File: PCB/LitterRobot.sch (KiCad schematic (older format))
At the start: 5 parts, among them J1 DF11C-4DP-2V(57), J2 DF11C-6DP-2V(57), J3 DF11C-8DP-2V(57), J4 DF11C-6DP-2V(57)

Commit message: Cleaned up the schematics
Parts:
- F1: value Polyfuse -> 1.1A; Voltage (none) -> 24V
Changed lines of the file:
@@
 TODO_1
-$Comp
-L Device:Polyfuse F1
-U 1 1 6061774B
-P 1250 2750
-F 0 "F1" H 1338 2796 50  0000 L CNN
-F 1 "Polyfuse" H 1338 2705 50  0000 L CNN
-F 2 "LitterRobot:Bel_Fuse_0ZCG" H 1300 2550 50  0001 L CNN
-F 3 "https://www.belfuse.com/resources/datasheets/circuitprotection/ds-cp-0zcg-series.pdf" H 1250 2750 50  0001 C CNN
-F 4 "0ZCG0110BF2B" H 1250 2750 50  0001 C CNN "Part_number"
-	1    1250 2750
-	1    0    0    -1
-$EndComp
 $Comp
 L power:+15V #PWR01
@@
 F32 "Light_sensor_SCL" O L 6000 2200 50
 F33 "Light_sensor_INT" I L 6000 2300 50
+F34 "Extension1" B L 6000 3100 50
+F35 "Extension2" B L 6000 3200 50
+F36 "Extension3" B L 6000 3300 50
+F37 "Extension4" B L 6000 3400 50
 $EndSheet
+$Comp
+L Device:Polyfuse F1
+U 1 1 6061774B
+P 1250 2750
+F 0 "F1" H 1338 2841 50  0000 L CNN
+F 1 "1.1A" H 1338 2750 50  0000 L CNN
+F 2 "LitterRobot:Bel_Fuse_0ZCG" H 1300 2550 50  0001 L CNN
+F 3 "https://www.belfuse.com/resources/datasheets/circuitprotection/ds-cp-0zcg-series.pdf" H 1250 2750 50  0001 C CNN
+F 4 "0ZCG0110BF2B" H 1250 2750 50  0001 C CNN "Part_number"
+F 5 "24V" H 1338 2659 50  0000 L CNN "Voltage"
+	1    1250 2750
+	1    0    0    -1
+$EndComp
+Wire Wire Line
+	6000 3200 5250 3200
+Wire Wire Line
+	6000 3100 5250 3100
+Wire Wire Line
+	6000 3400 5250 3400
+Wire Wire Line
+	6000 3300 5250 3300
+Text Label 5250 3100 0    50   ~ 0
+Extension1
+Text Label 5250 3200 0    50   ~ 0
+Extension2
+Text Label 5250 3300 0    50   ~ 0
+Extension3
+Text Label 5250 3400 0    50   ~ 0
+Extension4
 $EndSCHEMATC

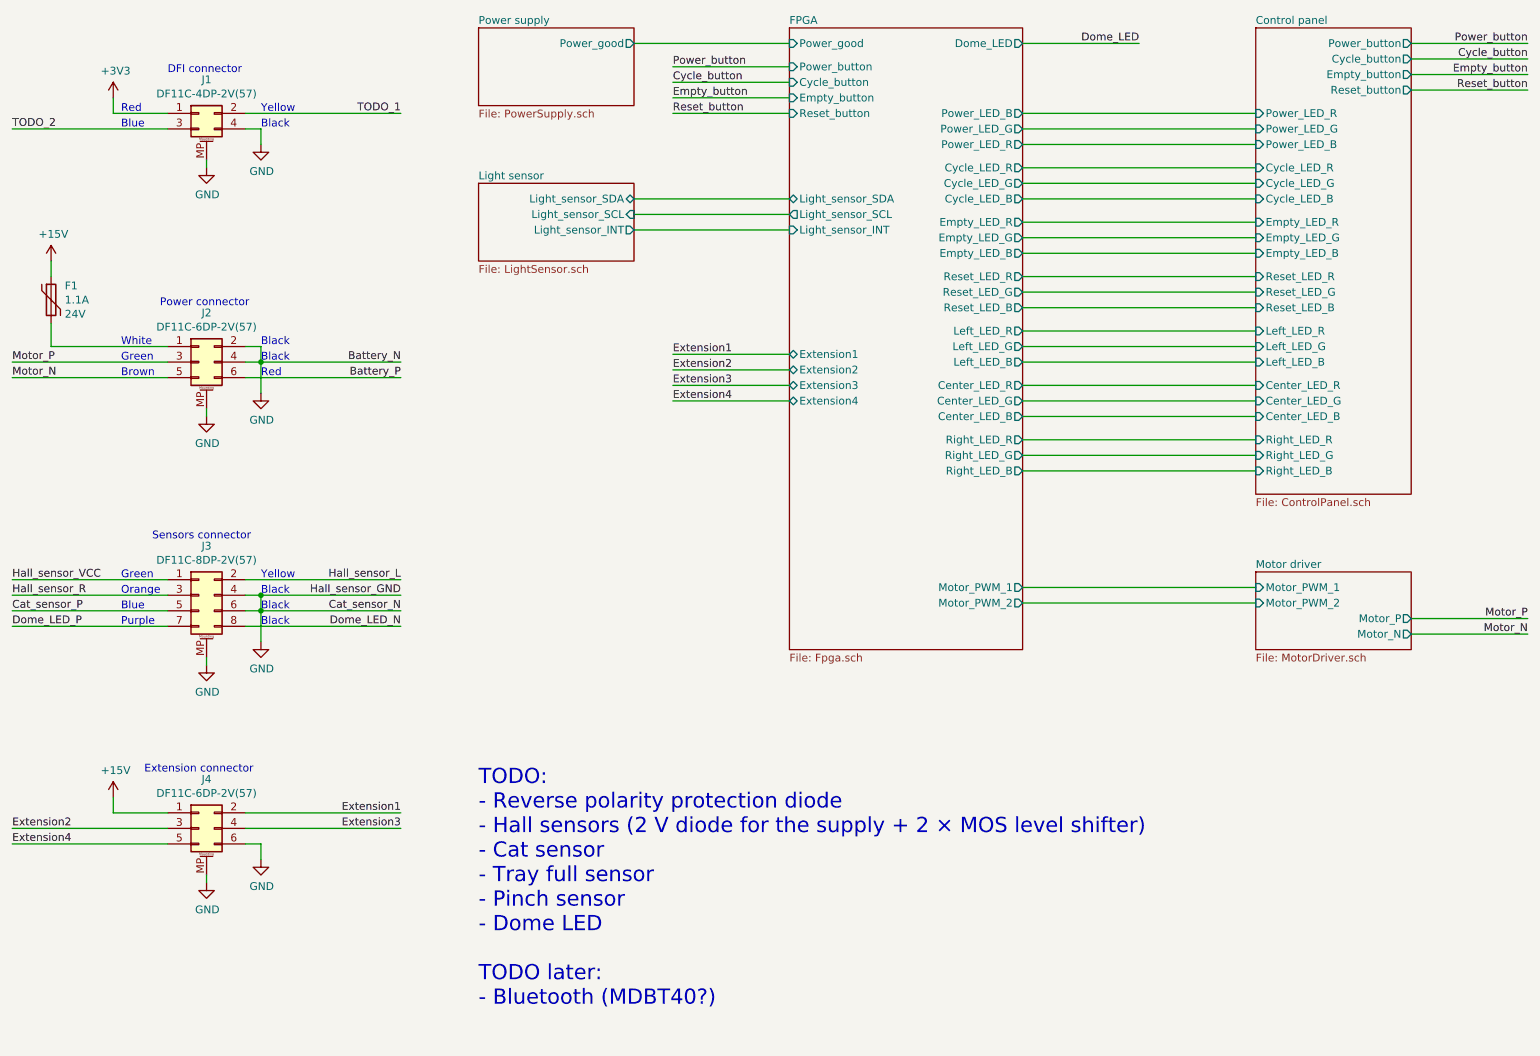
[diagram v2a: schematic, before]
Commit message: Add reverse polarity protection diodes
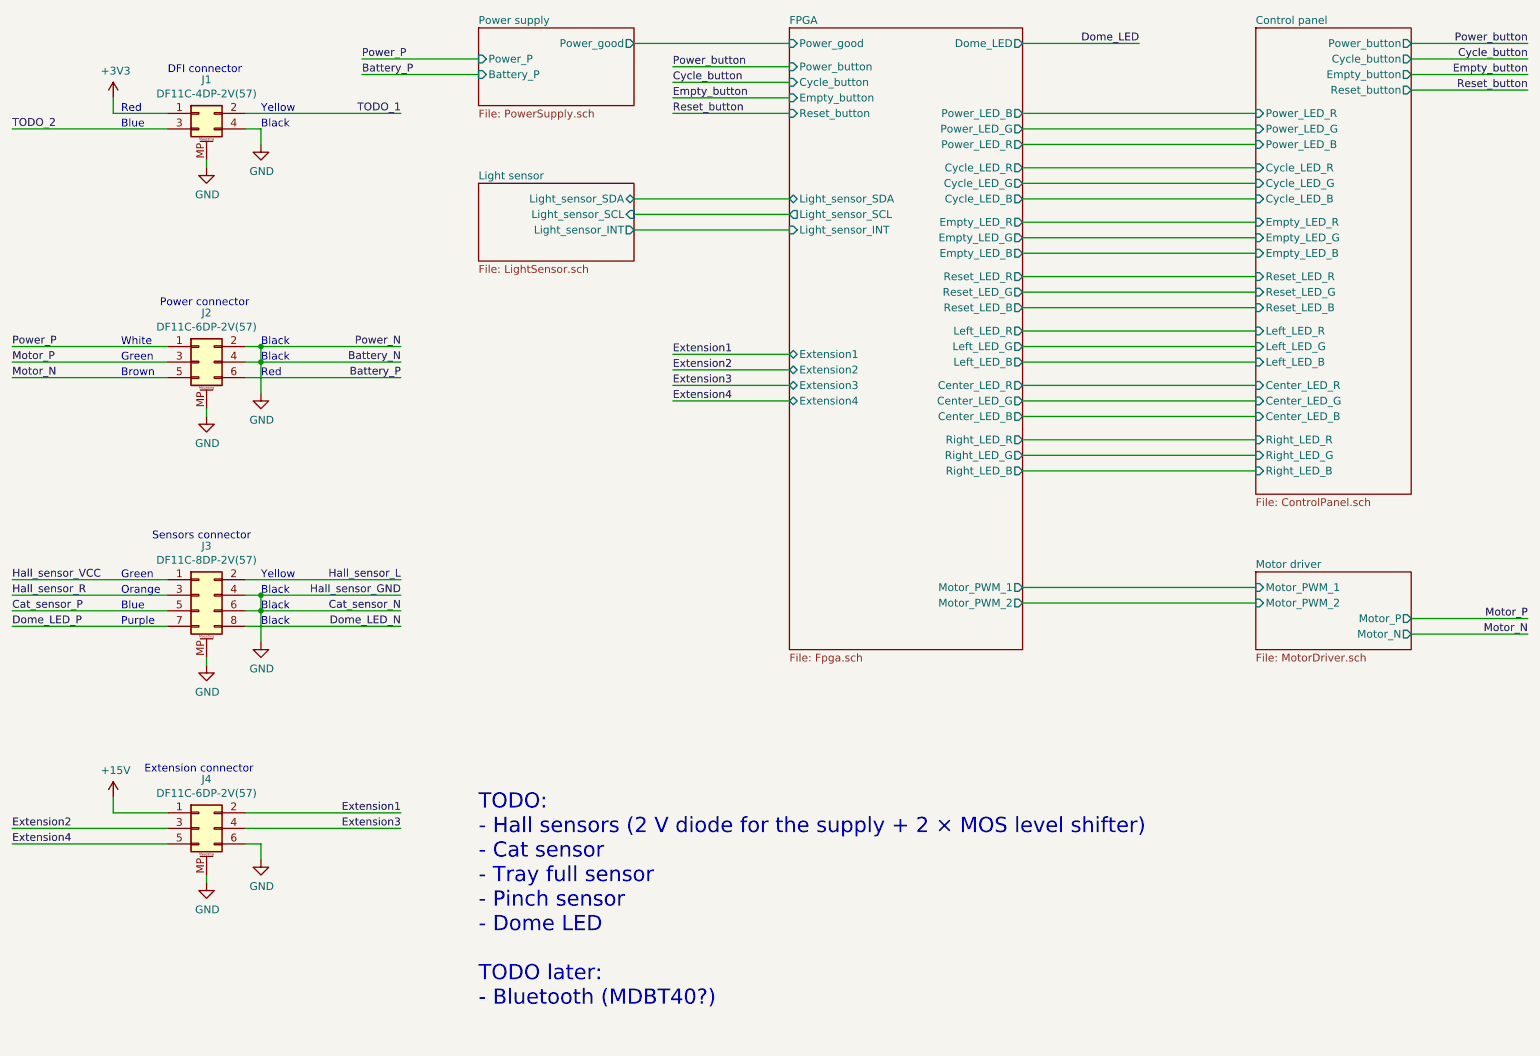
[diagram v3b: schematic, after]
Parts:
- removed F1: 1.1A, LitterRobot:Bel_Fuse_0ZCG, symbol Device:Polyfuse
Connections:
- net Power_P: now reaches J2.1 (Pin_1)
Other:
- note added: "TODO:\n- Hall sensors (2 V diode for the supply + 2 × MOS level shifter)\n- Cat sensor\n- Tray full sensor\n- Pinch sensor\n- Dome LED\n\nTODO later:\n- Bluetooth (MDBT40?)"
- note removed: "TODO:\n- Reverse polarity protection diode\n- Hall sensors (2 V diode for the supply + 2 × MOS level shifter)\n- Cat sensor\n- Tray full sensor\n- Pinch sensor\n- Dome LED\n\nTODO later:\n- Bluetooth (MDBT40?)"
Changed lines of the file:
@@
 F5 "Motor_N" O R 10000 4900 50
 $EndSheet
-Wire Wire Line
-	2500 3050 2600 3050
-Wire Wire Line
-	2600 3050 2600 3150
-$Comp
-L power:GND #PWR09
-U 1 1 6046CCE3
-P 2600 3350
-F 0 "#PWR09" H 2600 3100 50  0001 C CNN
-F 1 "GND" H 2605 3177 50  0000 C CNN
-F 2 "" H 2600 3350 50  0001 C CNN
-F 3 "" H 2600 3350 50  0001 C CNN
-	1    2600 3350
-	1    0    0    -1
-$EndComp
 Text Label 1000 3150 0    50   ~ 0
 Motor_P
@@
 $EndComp
 Wire Wire Line
-	2500 3150 2600 3150
-Connection ~ 2600 3150
-Wire Wire Line
-	2600 3150 2600 3350
-Wire Wire Line
 	2600 4750 2600 4950
 $Comp
@@
 	1    0    0    -1
 $EndComp
-Wire Wire Line
-	2600 3150 3500 3150
 Text Label 3500 3150 2    50   ~ 0
 Battery_N
@@
 F1 "PowerSupply.sch" 50
 F2 "Power_good" O R 5000 1100 50
+F3 "Power_P" I L 4000 1200 50
+F4 "Battery_P" I L 4000 1300 50
 $EndSheet
 Wire Wire Line
@@
 Text Label 3500 1550 2    50   ~ 0
 TODO_1
-$Comp
-L power:+15V #PWR01
-U 1 1 6046C18F
-P 1250 2500
-F 0 "#PWR01" H 1250 2350 50  0001 C CNN
-F 1 "+15V" H 1265 2673 50  0000 C CNN
-F 2 "" H 1250 2500 50  0001 C CNN
-F 3 "" H 1250 2500 50  0001 C CNN
-	1    1250 2500
-	1    0    0    -1
-$EndComp
-Wire Wire Line
-	1250 2500 1250 2600
-Wire Wire Line
-	1250 2900 1250 3050
-Wire Wire Line
-	1250 3050 2000 3050
 Text Notes 4000 7300 0    98   ~ 0
-TODO:\n- Reverse polarity protection diode\n- Hall sensors (2 V diode for the supply + 2 × MOS level shifter)\n- Cat sensor\n- Tray full sensor\n- Pinch sensor\n- Dome LED\n\nTODO later:\n- Bluetooth (MDBT40?)
+TODO:\n- Hall sensors (2 V diode for the supply + 2 × MOS level shifter)\n- Cat sensor\n- Tray full sensor\n- Pinch sensor\n- Dome LED\n\nTODO later:\n- Bluetooth (MDBT40?)
 Text Label 1000 4850 0    50   ~ 0
 Dome_LED_P
@@
 F37 "Extension4" B L 6000 3400 50
 $EndSheet
-$Comp
-L Device:Polyfuse F1
-U 1 1 6061774B
-P 1250 2750
-F 0 "F1" H 1338 2841 50  0000 L CNN
-F 1 "1.1A" H 1338 2750 50  0000 L CNN
-F 2 "LitterRobot:Bel_Fuse_0ZCG" H 1300 2550 50  0001 L CNN
-F 3 "https://www.belfuse.com/resources/datasheets/circuitprotection/ds-cp-0zcg-series.pdf" H 1250 2750 50  0001 C CNN
-F 4 "0ZCG0110BF2B" H 1250 2750 50  0001 C CNN "Part_number"
-F 5 "24V" H 1338 2659 50  0000 L CNN "Voltage"
-	1    1250 2750
-	1    0    0    -1
-$EndComp
 Wire Wire Line
 	6000 3200 5250 3200
@@
 Text Label 5250 3400 0    50   ~ 0
 Extension4
+Wire Wire Line
+	4000 1300 3250 1300
+Wire Wire Line
+	4000 1200 3250 1200
+Text Label 3250 1200 0    50   ~ 0
+Power_P
+Text Label 3250 1300 0    50   ~ 0
+Battery_P
+Wire Wire Line
+	1000 3050 2000 3050
+Text Label 1000 3050 0    50   ~ 0
+Power_P
+Text Label 3500 3050 2    50   ~ 0
+Power_N
+$Comp
+L power:GND #PWR09
+U 1 1 6046CCE3
+P 2600 3350
+F 0 "#PWR09" H 2600 3100 50  0001 C CNN
+F 1 "GND" H 2605 3177 50  0000 C CNN
+F 2 "" H 2600 3350 50  0001 C CNN
+F 3 "" H 2600 3350 50  0001 C CNN
+	1    2600 3350
+	1    0    0    -1
+$EndComp
+Wire Wire Line
+	2600 3150 3500 3150
+Wire Wire Line
+	2500 3150 2600 3150
+Connection ~ 2600 3150
+Wire Wire Line
+	2600 3150 2600 3350
+Wire Wire Line
+	3500 3050 2600 3050
+Wire Wire Line
+	2500 3050 2600 3050
+Connection ~ 2600 3050
+Wire Wire Line
+	2600 3050 2600 3150
 $EndSCHEMATC

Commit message: Add support for the weight sensor
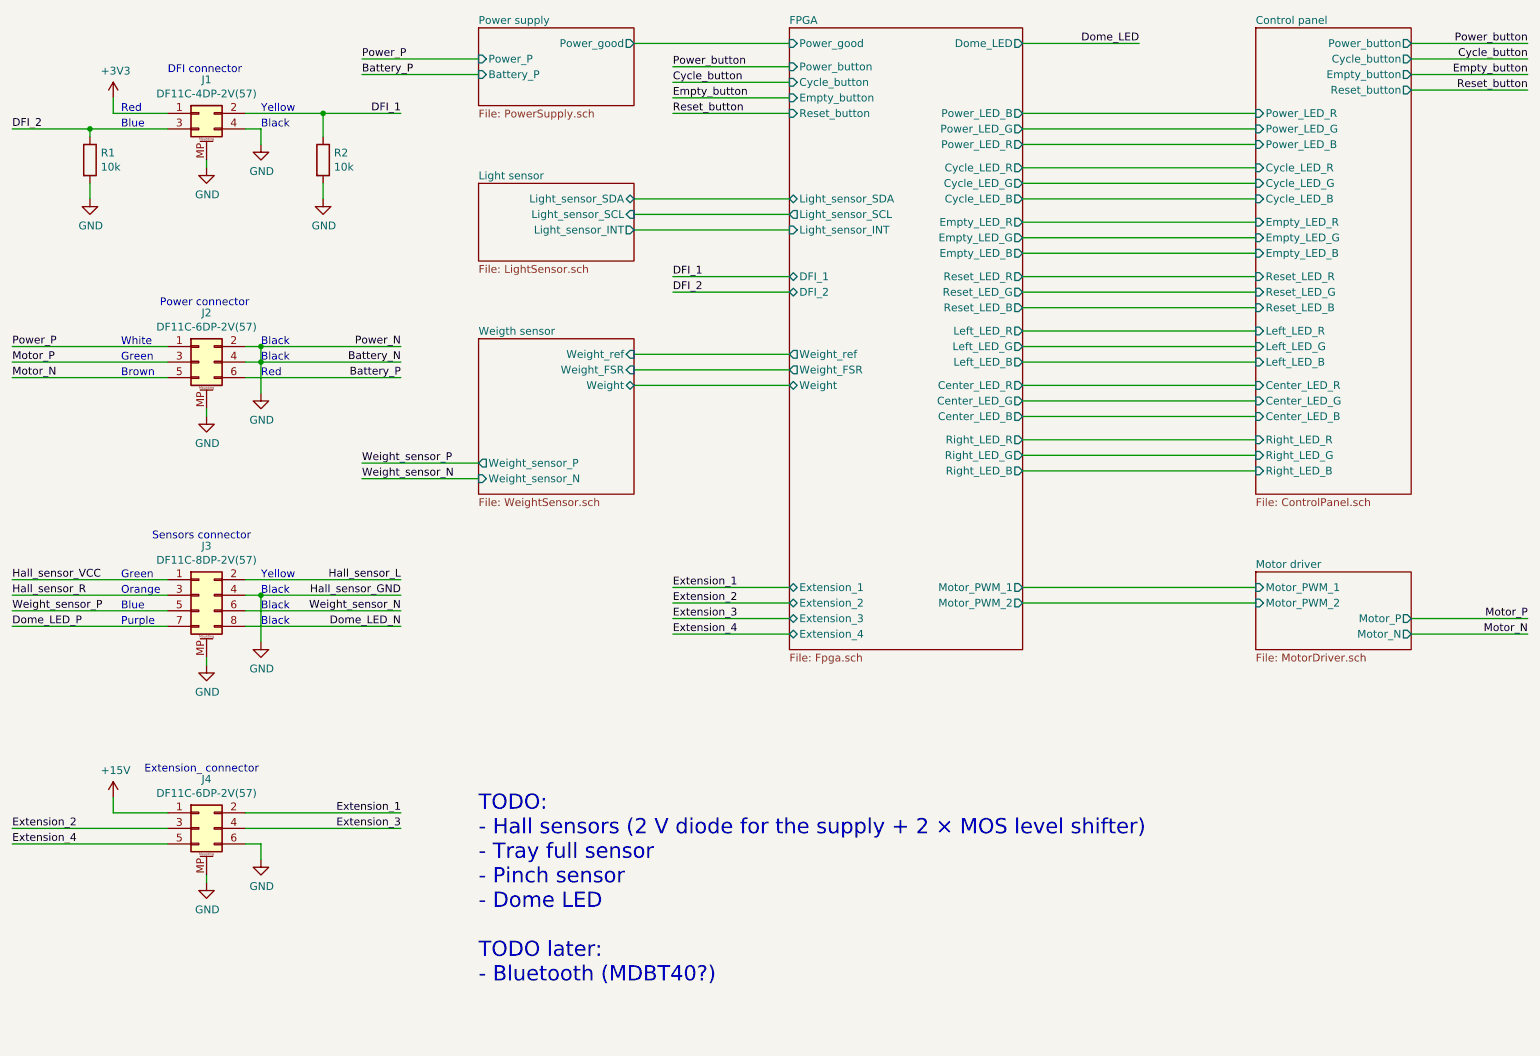
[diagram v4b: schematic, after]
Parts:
- added R1, R2: 10k, Resistor_SMD:R_0603_1608Metric, symbol Device:R
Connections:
- net GND: now also R1.2, R2.2; no longer J3.6 (Pin_6)
- net Cat_sensor_P renamed Weight_sensor_P
- net Extension1 renamed Extension_1
- net Extension2 renamed Extension_2
- net Extension3 renamed Extension_3
- net Extension4 renamed Extension_4
- net TODO_1 renamed DFI_1
- net DFI_1: now also R2.1
- net TODO_2 renamed DFI_2
- net DFI_2: now also R1.1
- new net Weight_sensor_N: J3.6 (Pin_6)
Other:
- note added: "Extension_ connector"
- note added: "TODO:\n- Hall sensors (2 V diode for the supply + 2 × MOS level shifter)\n- Tray full sensor\n- Pinch sensor\n- Dome LED\n\nTODO later:\n- Bluetooth (MDBT40?)"
- note removed: "Extension connector"
- note removed: "TODO:\n- Hall sensors (2 V diode for the supply + 2 × MOS level shifter)\n- Cat sensor\n- Tray full sensor\n- Pinch sensor\n- Dome LED\n\nTODO later:\n- Bluetooth (MDBT40?)"
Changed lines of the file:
@@
 $Descr A4 11693 8268
 encoding utf-8
-Sheet 1 19
+Sheet 1 20
 Title "Litter Robot 3 - Main board"
-Date "2021-03-28"
+Date "2021-04-02"
 Rev "A1"
 Comp "L. Sartory"
@@
 Wire Wire Line
 	2500 4650 2600 4650
-Wire Wire Line
-	2600 4650 2600 4750
-Wire Wire Line
-	2500 4750 2600 4750
-Connection ~ 2600 4750
 Text Notes 2600 3250 0    50   ~ 0
 Red
@@
 $EndComp
 Text Notes 1850 5800 0    50   ~ 0
-Extension connector
+Extension_ connector
 $Sheet
 S 9000 4500 1000 500
@@
 	1    0    0    -1
 $EndComp
-Wire Wire Line
-	2600 4750 2600 4950
 $Comp
 L power:GND #PWR08
@@
 	1000 6250 2000 6250
 Text Label 3500 6050 2    50   ~ 0
-Extension1
+Extension_1
 Text Label 1000 6150 0    50   ~ 0
-Extension2
+Extension_2
 Text Label 3500 6150 2    50   ~ 0
-Extension3
+Extension_3
 Text Label 1000 6250 0    50   ~ 0
-Extension4
+Extension_4
 Wire Wire Line
 	2600 4650 3500 4650
@@
 Wire Wire Line
 	2500 4850 3500 4850
-Wire Wire Line
-	2600 4750 3500 4750
 Wire Wire Line
 	7500 1550 9000 1550
@@
 	1000 4750 2000 4750
 Text Label 1000 4750 0    50   ~ 0
-Cat_sensor_P
+Weight_sensor_P
 Wire Wire Line
 	5000 1100 6000 1100
 Wire Wire Line
-	2500 1550 3500 1550
-Wire Wire Line
-	1000 1650 2000 1650
+	2500 1550 3000 1550
+Wire Wire Line
+	1000 1650 1500 1650
 Text Label 1000 1650 0    50   ~ 0
-TODO_2
+DFI_2
 Text Label 3500 1550 2    50   ~ 0
-TODO_1
-Text Notes 4000 7300 0    98   ~ 0
-TODO:\n- Hall sensors (2 V diode for the supply + 2 × MOS level shifter)\n- Cat sensor\n- Tray full sensor\n- Pinch sensor\n- Dome LED\n\nTODO later:\n- Bluetooth (MDBT40?)
+DFI_1
+Text Notes 4000 7150 0    98   ~ 0
+TODO:\n- Hall sensors (2 V diode for the supply + 2 × MOS level shifter)\n- Tray full sensor\n- Pinch sensor\n- Dome LED\n\nTODO later:\n- Bluetooth (MDBT40?)
 Text Label 1000 4850 0    50   ~ 0
 Dome_LED_P
 Text Label 3500 4750 2    50   ~ 0
-Cat_sensor_N
+Weight_sensor_N
 Text Label 3500 4850 2    50   ~ 0
 Dome_LED_N
@@
 F32 "Light_sensor_SCL" O L 6000 2200 50
 F33 "Light_sensor_INT" I L 6000 2300 50
-F34 "Extension1" B L 6000 3100 50
-F35 "Extension2" B L 6000 3200 50
-F36 "Extension3" B L 6000 3300 50
-F37 "Extension4" B L 6000 3400 50
+F34 "Extension_1" B L 6000 4600 50
+F35 "Extension_2" B L 6000 4700 50
+F36 "Extension_3" B L 6000 4800 50
+F37 "Extension_4" B L 6000 4900 50
+F38 "DFI_1" B L 6000 2600 50
+F39 "DFI_2" B L 6000 2700 50
+F40 "Weight" T L 6000 3300 50
+F41 "Weight_ref" O L 6000 3100 50
+F42 "Weight_FSR" O L 6000 3200 50
 $EndSheet
 Wire Wire Line
-	6000 3200 5250 3200
-Wire Wire Line
-	6000 3100 5250 3100
-Wire Wire Line
-	6000 3400 5250 3400
-Wire Wire Line
-	6000 3300 5250 3300
-Text Label 5250 3100 0    50   ~ 0
-Extension1
-Text Label 5250 3200 0    50   ~ 0
-Extension2
-Text Label 5250 3300 0    50   ~ 0
-Extension3
-Text Label 5250 3400 0    50   ~ 0
-Extension4
+	6000 4700 5250 4700
+Wire Wire Line
+	6000 4600 5250 4600
+Wire Wire Line
+	6000 4900 5250 4900
+Wire Wire Line
+	6000 4800 5250 4800
+Text Label 5250 4600 0    50   ~ 0
+Extension_1
+Text Label 5250 4700 0    50   ~ 0
+Extension_2
+Text Label 5250 4800 0    50   ~ 0
+Extension_3
+Text Label 5250 4900 0    50   ~ 0
+Extension_4
 Wire Wire Line
 	4000 1300 3250 1300
@@
 Wire Wire Line
 	2600 3050 2600 3150
+$Comp
+L Device:R R?
+U 1 1 6068BE20
+P 1500 1850
+AR Path="/603F20AB/6068BE20" Ref="R?"  Part="1"
+AR Path="/603F1DCE/6068BE20" Ref="R?"  Part="1"
+AR Path="/60624089/6068BE20" Ref="R?"  Part="1"
+AR Path="/603F1F4D/60647CC2/6068BE20" Ref="R?"  Part="1"
+AR Path="/6068BE20" Ref="R1"  Part="1"
+F 0 "R1" H 1570 1896 50  0000 L CNN
+F 1 "10k" H 1570 1805 50  0000 L CNN
+F 2 "Resistor_SMD:R_0603_1608Metric" V 1430 1850 50  0001 C CNN
+F 3 "https://www.bourns.com/docs/product-datasheets/CRxxxxx.pdf" H 1500 1850 50  0001 C CNN
+F 4 "CR0603-FX-1002ELF" H 1500 1850 50  0001 C CNN "Part_number"
+	1    1500 1850
+	1    0    0    -1
+$EndComp
+$Comp
+L Device:R R?
+U 1 1 6068EA07
+P 3000 1850
+AR Path="/603F20AB/6068EA07" Ref="R?"  Part="1"
+AR Path="/603F1DCE/6068EA07" Ref="R?"  Part="1"
+AR Path="/60624089/6068EA07" Ref="R?"  Part="1"
+AR Path="/603F1F4D/60647CC2/6068EA07" Ref="R?"  Part="1"
+AR Path="/6068EA07" Ref="R2"  Part="1"
+F 0 "R2" H 3070 1896 50  0000 L CNN
+F 1 "10k" H 3070 1805 50  0000 L CNN
+F 2 "Resistor_SMD:R_0603_1608Metric" V 2930 1850 50  0001 C CNN
+F 3 "https://www.bourns.com/docs/product-datasheets/CRxxxxx.pdf" H 3000 1850 50  0001 C CNN
+F 4 "CR0603-FX-1002ELF" H 3000 1850 50  0001 C CNN "Part_number"
+	1    3000 1850
+	1    0    0    -1
+$EndComp
+$Comp
+L power:GND #PWR01
+U 1 1 6068F29F
+P 1500 2100
+F 0 "#PWR01" H 1500 1850 50  0001 C CNN
+F 1 "GND" H 1505 1927 50  0000 C CNN
+F 2 "" H 1500 2100 50  0001 C CNN
+F 3 "" H 1500 2100 50  0001 C CNN
+	1    1500 2100
+	1    0    0    -1
+$EndComp
+$Comp
+L power:GND #PWR012
+U 1 1 6068F7E3
+P 3000 2100
+F 0 "#PWR012" H 3000 1850 50  0001 C CNN
+F 1 "GND" H 3005 1927 50  0000 C CNN
+F 2 "" H 3000 2100 50  0001 C CNN
+F 3 "" H 3000 2100 50  0001 C CNN
+	1    3000 2100
+	1    0    0    -1
+$EndComp
+Wire Wire Line
+	3000 2100 3000 2000
+Wire Wire Line
+	3000 1700 3000 1550
+Connection ~ 3000 1550
+Wire Wire Line
+	3000 1550 3500 1550
+Wire Wire Line
+	1500 2100 1500 2000
+Wire Wire Line
+	1500 1700 1500 1650
+Connection ~ 1500 1650
+Wire Wire Line
+	1500 1650 2000 1650
+Wire Wire Line
+	6000 2700 5250 2700
+Wire Wire Line
+	6000 2600 5250 2600
+Text Label 5250 2600 0    50   ~ 0
+DFI_1
+Text Label 5250 2700 0    50   ~ 0
+DFI_2
+$Sheet
+S 4000 3000 1000 1000
+U 606A580A
+F0 "Weigth sensor" 50
+F1 "WeightSensor.sch" 50
+F2 "Weight_sensor_P" O L 4000 3800 50
+F3 "Weight_sensor_N" I L 4000 3900 50
+F4 "Weight_ref" I R 5000 3100 50
+F5 "Weight_FSR" I R 5000 3200 50
+F6 "Weight" T R 5000 3300 50
+$EndSheet
+Wire Wire Line
+	2600 4650 2600 4950
+Wire Wire Line
+	2500 4750 3500 4750
+Wire Wire Line
+	4000 3900 3250 3900
+Wire Wire Line
+	4000 3800 3250 3800
+Text Label 3250 3800 0    50   ~ 0
+Weight_sensor_P
+Text Label 3250 3900 0    50   ~ 0
+Weight_sensor_N
+Wire Wire Line
+	5000 3100 6000 3100
+Wire Wire Line
+	6000 3200 5000 3200
+Wire Wire Line
+	5000 3300 6000 3300
 $EndSCHEMATC
